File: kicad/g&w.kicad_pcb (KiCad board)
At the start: 4 copper layers, 108.7 x 55.1 mm, 193 parts, among them IC1 NAU8315-B31V, IC2 MX25U8035FM2, IC3 LD39020DTPU33R, IC4 DA9230-61VZ2, IC5 BQ24072RGT, J1 speaker, J2 SWD PORT, J3 DISPLAY1, J4 DISPLAY2, J5 Battery, J6 USB-C, Q1 PMBT3904, Q2 PMBT3904, Q3 PMBT3904, Q4 SSM6J412TU, Y1 H01717

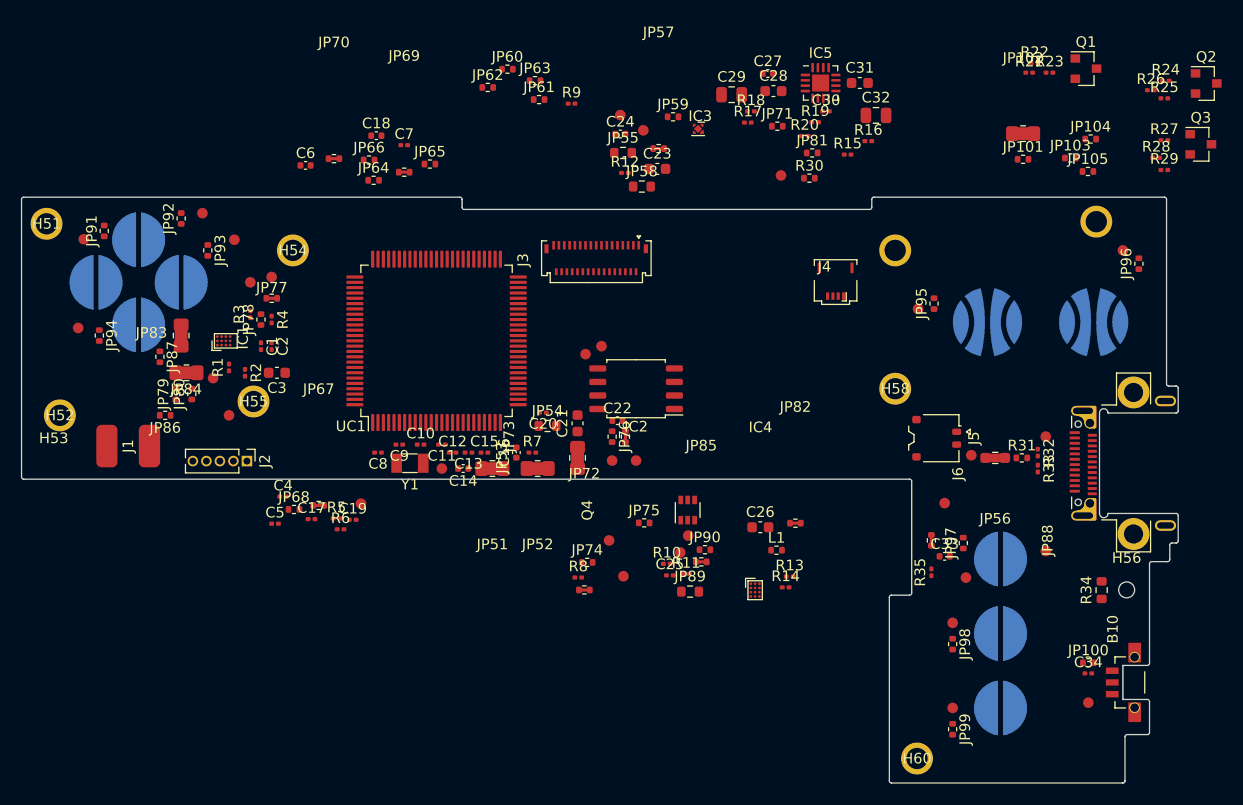
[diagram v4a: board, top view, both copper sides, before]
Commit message: all footprints placed, a very rough dxf graphics layer was made to locate most components, several footprints were tweaked and a few missing from the schematic were added and will be in the next revision.
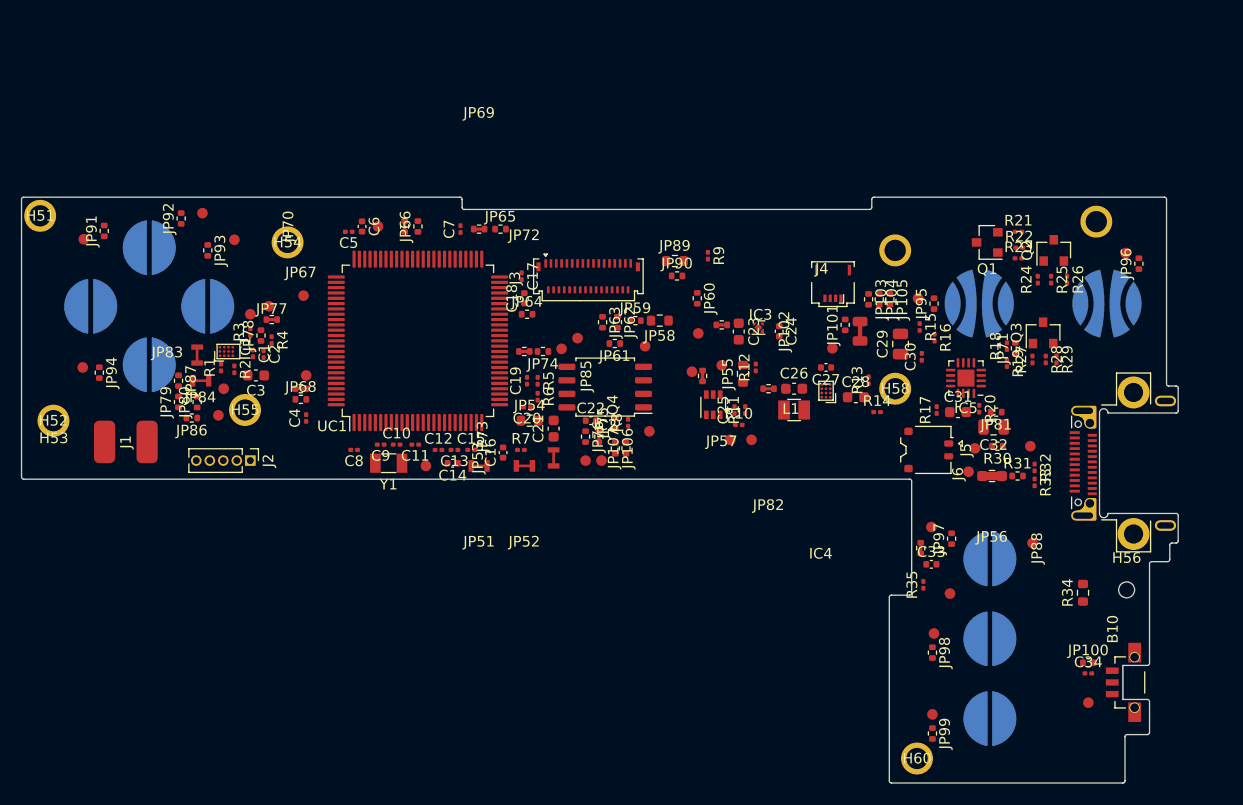
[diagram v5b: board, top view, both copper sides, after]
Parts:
- added JP106: JMP-0402-OPEN, Resistor_SMD:R_0402_1005Metric, F.Cu at (55.8, 23.6)
- added JP107: JMP-0402-OPEN, Resistor_SMD:R_0402_1005Metric, F.Cu at (56.8, 23.6)
- added TP82: TestPoint, gnw:gnw-TestPoint_Pad_D1.0mm, F.Cu at (33.5, 2.75)
- added TP83: TestPoint, gnw:gnw-TestPoint_Pad_D1.0mm, F.Cu at (26.5, 9.25)
- added TP84: TestPoint, gnw:gnw-TestPoint_Pad_D1.0mm, F.Cu at (68.6, 22.8)
- added TP85: TestPoint, gnw:gnw-TestPoint_Pad_D1.0mm, F.Cu at (76.2, 14.2)
- L1: footprint Resistor_SMD:R_0402_1005Metric -> gnw:L_0806_2016Metric
- moved R18 32.6 mm to (92.6, 14.0), turned to 90 degrees
- moved R17 32.3 mm to (86.0, 20.0), turned to 90 degrees
- moved C31 32.3 mm to (88.0, 20.2)
- moved TP70 31.5 mm to (89.6, 23.6)
- moved C32 31.3 mm to (91.3, 21.6), turned to 180 degrees
- moved JP89 31.1 mm to (61.4, 6.00)
- moved IC5 30.9 mm to (88.8, 17.0), turned to 180 degrees
- moved R30 30.8 mm to (91.7, 23.4), turned to 180 degrees
- moved JP71 30.6 mm to (93.4, 14.2), turned to 90 degrees
- moved R20 30.4 mm to (90.0, 19.9), turned to 270 degrees
- moved C17 30.2 mm to (47.0, 7.43), turned to 270 degrees
- moved JP81 29.9 mm to (91.6, 20.2), turned to 180 degrees
- moved C28 29.8 mm to (78.4, 18.8)
- moved R19 28.9 mm to (92.6, 15.6), turned to 270 degrees
- moved C29 28.3 mm to (82.6, 13.8), turned to 90 degrees
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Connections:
- C26 pad 1: V1v8 -> Net-(C26-Pad1)
- IC4 pad B3: Net-(IC4-PadB3) -> V1v8
- JP82 pad 1: Net-(IC4-PadB3) -> Net-(C26-Pad1)
- L1 pad 2: Net-(IC4-PadB3) -> Net-(C26-Pad1)

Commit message: about 1/3rd routed
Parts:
- moved TP73 3.26 mm to (19.8, 3.25)
- moved JP92 3.01 mm to (17.0, 4.25)
- moved JP91 2.35 mm to (7.50, 5.50)
- moved TP74 2.15 mm to (21.2, 5.75)
- moved TP72 2.08 mm to (5.50, 6.00)
- moved JP93 1.95 mm to (19.0, 6.24)
- moved JP79 1.77 mm to (16.5, 19.0)
- moved JP87 1.53 mm to (14.2, 18.7)
- moved TP68 1.43 mm to (86.1, 29.7)
- moved R33 1.25 mm to (96.2, 26.1)
- moved R31 1.23 mm to (94.6, 25.4)
- moved JP56 1.23 mm to (92.2, 25.4)
- moved R32 1.21 mm to (96.2, 24.7)
- moved R1 1.18 mm to (19.9, 16.3)
- moved R2 1.11 mm to (21.0, 16.6)
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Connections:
- B10 pad 1: b10p22-PA0 -> GND
- B10 pad 2: GND -> b10p22-PA0
- B10 pad MP: (no net) -> GND
- J4 pad 1: Net-(J4-Pad1) -> xV3v7
- JP101 pad 2: Net-(J4-Pad1) -> xV3v7
- JP102 pad 2: Net-(J4-Pad1) -> xV3v7
- JP103 pad 2: V3v7 -> xV3v7
- JP104 pad 2: V3v7 -> xV3v7
- JP105 pad 2: V3v7 -> xV3v7
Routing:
- net GND: track 0.00 -> 207.0 mm, vias 0 -> 28
- net V1v8: track 0.00 -> 55.2 mm, vias 0 -> 13
- net V3v7: track 0.00 -> 52.8 mm, vias 0 -> 2
- net f1p41-PE11: track 0.00 -> 24.1 mm, vias 0 -> 2
- net Net-(IC5-Pad1): track 0.00 -> 21.4 mm, vias 0 -> 2
- net Vusb: track 0.00 -> 20.1 mm, vias 0 -> 4
- net Net-(J6-PadA4): track 0.00 -> 17.5 mm
- net Net-(J1-Pad1): track 0.00 -> 13.8 mm
- net b10p22-PA0: track 0.00 -> 13.6 mm, vias 0 -> 2
- net V3v3: track 0.00 -> 12.8 mm, vias 0 -> 2
- net VBAT: track 0.00 -> 12.3 mm, vias 0 -> 1
- net p27-VDD: track 0.00 -> 10.8 mm, vias 0 -> 1
- net Net-(IC2-Pad7): track 0.00 -> 10.7 mm
- net f3p1-PE2: track 0.00 -> 10.6 mm, vias 0 -> 1
- net Vaux1v8: track 0.00 -> 10.00 mm, vias 0 -> 3
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
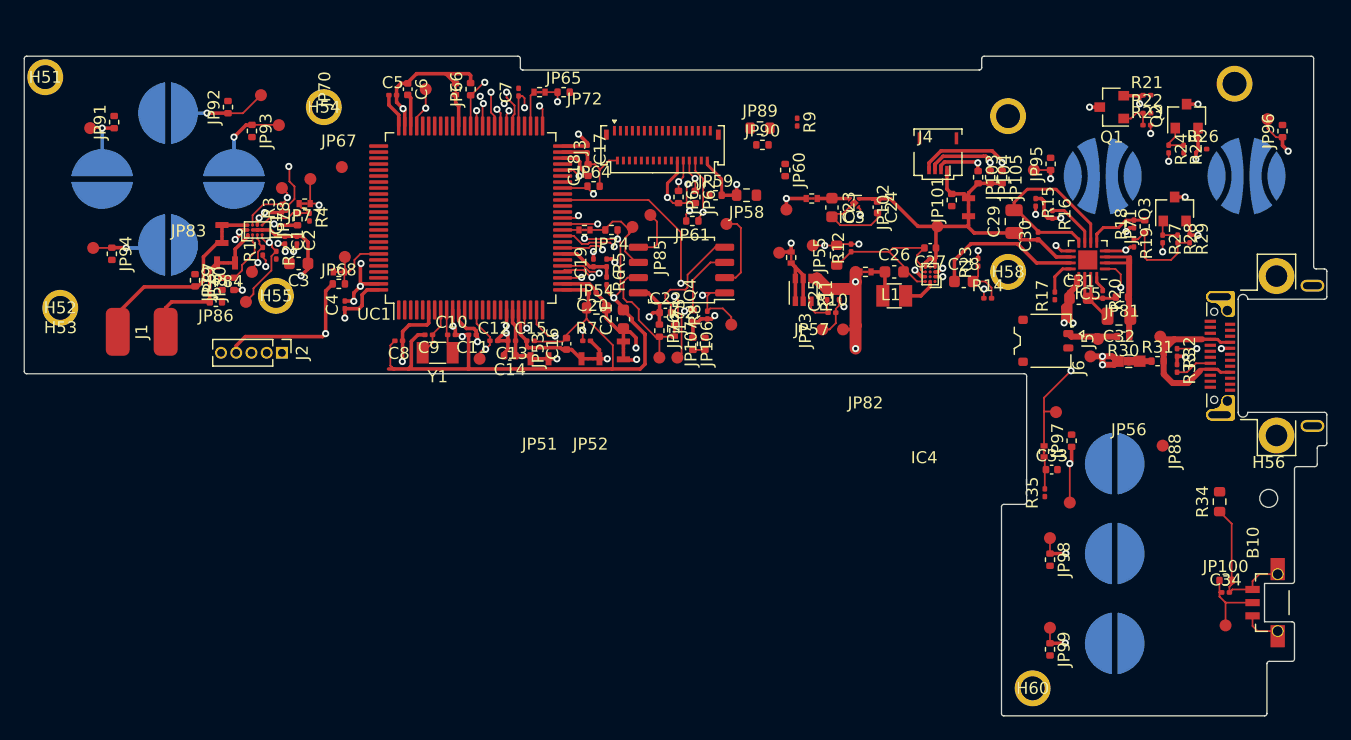
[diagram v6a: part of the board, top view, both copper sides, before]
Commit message: first draft: full retrace of interior traces and ground plane. Also the board is designed for 3 layers, No routing conflicts found.
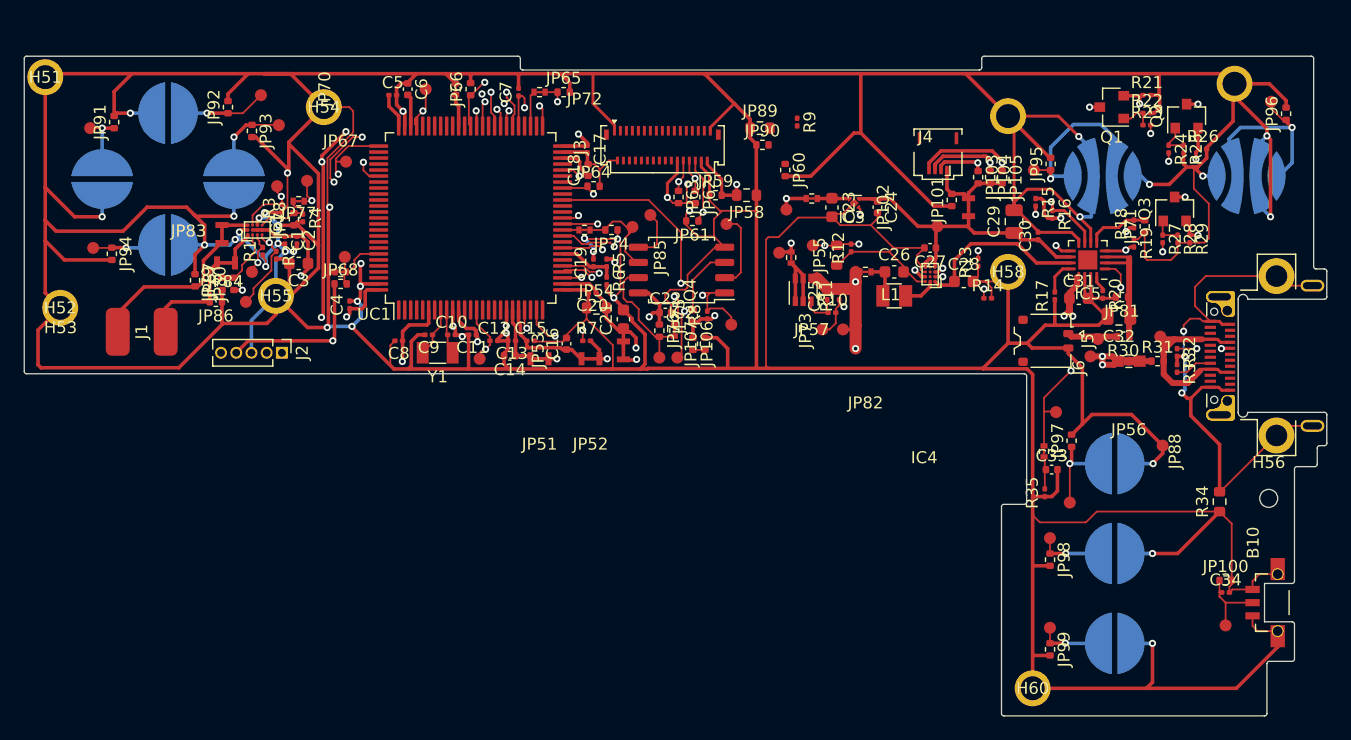
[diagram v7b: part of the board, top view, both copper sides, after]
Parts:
- moved JP96 1.48 mm to (105.3, 4.80)
- moved TP77 1.48 mm to (104.0, 3.80)
- moved TP83 0.57 mm to (26.9, 8.80)
- moved R4 0.55 mm to (23.2, 13.5)
- moved JP77 0.54 mm to (22.9, 12.1)
- moved TP60 0.43 mm to (21.1, 10.8)
- moved C4 0.40 mm to (27.1, 20.8)
- moved TP59 0.31 mm to (23.6, 10.4)
- moved JP78 0.30 mm to (22.5, 13.6)
- moved JP67 0.15 mm to (26.4, 18.0)
- moved JP68 0.15 mm to (26.4, 19.0)
- turned B6 to 180 degrees
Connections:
- B10 pad MP: GND -> (no net)
- J6 pad A1: Net-(J6-PadA1) -> usbGND
- J6 pad A12: Net-(J6-PadA1) -> usbGND
- J6 pad B1: Net-(J6-PadA1) -> usbGND
- J6 pad B12: Net-(J6-PadA1) -> usbGND
- J6 pad S1: Net-(J6-PadA1) -> usbGND
- R32 pad 2: GND -> usbGND
- R33 pad 1: GND -> usbGND
- R34 pad 2: Net-(J6-PadA1) -> usbGND
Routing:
- net GND: track 207.0 -> 855.4 mm, vias 28 -> 43
- net usbGND: track 0.00 -> 48.9 mm, vias 0 -> 3
- net b1p58-PD11: track 5.52 -> 41.9 mm
- net SWDIO-p72-PA13: track 3.39 -> 35.3 mm, vias 1 -> 3
- net b4p81-PD0: track 4.20 -> 32.3 mm, vias 1 -> 2
- net SWCLK-p76-PA14: track 0.00 -> 26.5 mm, vias 0 -> 1
- net b2p61-PD14: track 7.88 -> 33.4 mm
- net b3p62-PD15: track 6.53 -> 28.7 mm
- net V1v8: track 55.2 -> 74.0 mm, vias 13 -> 16
- net RESET-p14-NRST: track 5.01 -> 23.1 mm
- net b5p86-PD5: track 2.13 -> 16.8 mm
- net b6p56-PD9: track 6.87 -> 19.8 mm
- net V3v7: track 52.8 -> 54.7 mm
- net b9p16-PC1: track 2.57 -> 4.31 mm
- net b8p33-PC5: track 6.14 -> 7.82 mm
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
